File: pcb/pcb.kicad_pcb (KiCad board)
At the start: 2 copper layers, 11 parts, among them J1 pin_header, J2 power_jack_socket

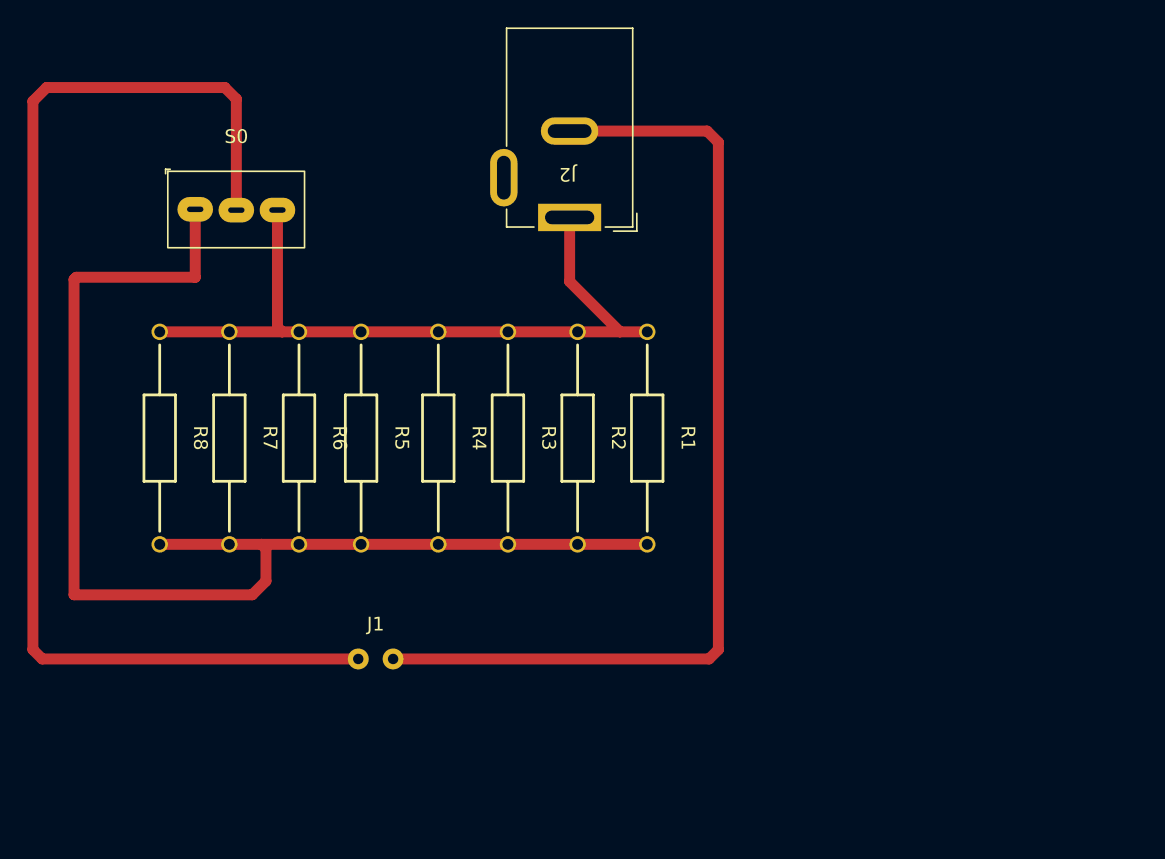
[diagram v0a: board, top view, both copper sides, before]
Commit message: add 3d render
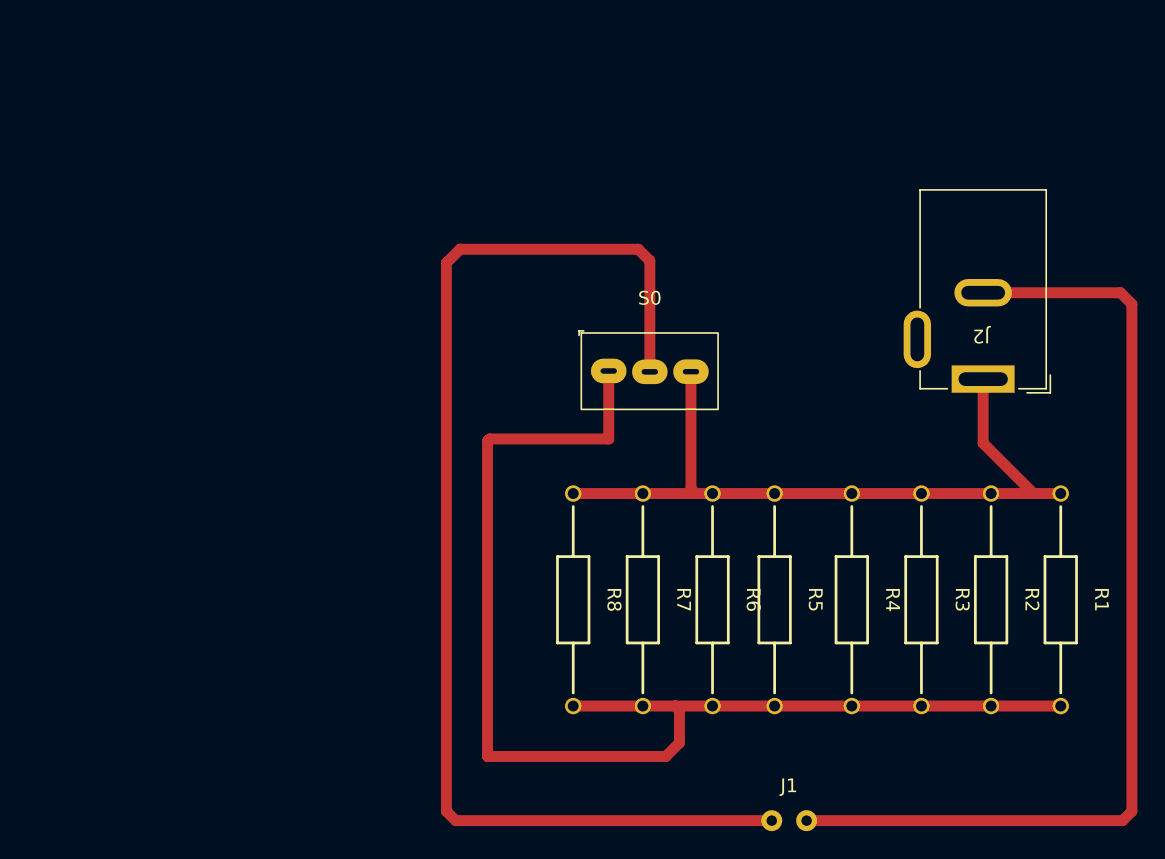
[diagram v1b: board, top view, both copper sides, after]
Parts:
- moved J2 32.4 mm to (171.4, 78.7)
- moved S0 32.4 mm to (147.0, 85.5)
- moved J1 32.4 mm to (157.2, 118.5)
- moved R1 32.4 mm to (176.9, 102.4)
- moved R2 32.4 mm to (171.9, 102.4)
- moved R3 32.4 mm to (166.8, 102.4)
- moved R4 32.4 mm to (161.7, 102.4)
- moved R5 32.4 mm to (156.1, 102.4)
- moved R6 32.4 mm to (151.5, 102.4)
- moved R8 32.4 mm to (141.4, 102.4)
- moved R7 32.4 mm to (146.5, 102.4)
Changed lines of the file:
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@@
   (net 5 "Net-(R1-Pad2)")
   (footprint "Library:100_ohm_resistor" (layer "F.Cu")
-    (at 141.7 90.56 -90)
+    (at 171.861956 102.353478 -90)
     (property "Sheetfile" "pcb.kicad_sch")
     (property "Sheetname" "")
@@
   )
   (footprint "Library:100_ohm_resistor" (layer "F.Cu")
-    (at 116.3 90.56 -90)
+    (at 146.461956 102.353478 -90)
     (property "Sheetfile" "pcb.kicad_sch")
     (property "Sheetname" "")
@@
   )
   (footprint "Library:100_ohm_resistor" (layer "F.Cu")
-    (at 121.38 90.56 -90)
+    (at 151.541956 102.353478 -90)
     (property "Sheetfile" "pcb.kicad_sch")
     (property "Sheetname" "")
@@
   )
   (footprint "Library:slide_switch" (layer "F.Cu")
-    (at 116.84 73.66)
+    (at 147.001956 85.453478)
     (property "Sheetfile" "pcb.kicad_sch")
     (property "Sheetname" "")
@@
   )
   (footprint "Library:100_ohm_resistor" (layer "F.Cu")
-    (at 131.54 90.56 -90)
+    (at 161.701956 102.353478 -90)
     (property "Sheetfile" "pcb.kicad_sch")
     (property "Sheetname" "")
@@
   )
   (footprint "Library:100_ohm_resistor" (layer "F.Cu")
-    (at 111.22 90.56 -90)
+    (at 141.381956 102.353478 -90)
     (property "Sheetfile" "pcb.kicad_sch")
     (property "Sheetname" "")
@@
   )
   (footprint "Library:100_ohm_resistor" (layer "F.Cu")
-    (at 136.62 90.56 -90)
+    (at 166.781956 102.353478 -90)
     (property "Sheetfile" "pcb.kicad_sch")
     (property "Sheetname" "")
@@
   )
   (footprint "Library:power_jack_socket" (layer "F.Cu")
-    (at 141.23 66.955 180)
+    (at 171.391956 78.748478 180)
     (property "Sheetfile" "pcb.kicad_sch")
     (property "Sheetname" "")
@@
   )
   (footprint "Library:100_ohm_resistor" (layer "F.Cu")
-    (at 146.78 90.56 -90)
+    (at 176.941956 102.353478 -90)
     (property "Sheetfile" "pcb.kicad_sch")
     (property "Sheetname" "")
@@
   )
   (footprint "Library:100_ohm_resistor" (layer "F.Cu")
-    (at 125.9092 90.56 -90)
+    (at 156.071156 102.353478 -90)
     (property "Sheetfile" "pcb.kicad_sch")
     (property "Sheetname" "")
@@
   )
   (footprint "Library:pin_header" (layer "F.Cu")
-    (at 127 106.68)
+    (at 157.161956 118.473478)
     (property "Sheetfile" "pcb.kicad_sch")
     (property "Sheetname" "")
@@
     )
   )
-  (gr_rect (start 99 63) (end 155 112) (layer "F.CrtYd") (width 0.05) (fill none))
-  (segment (start 116.8375 73.9425) (end 116.8375 65.8375) (width 0.8) (layer "F.Cu") (net 1))
-  (segment (start 103 65) (end 102 66) (width 0.8) (layer "F.Cu") (net 1))
-  (segment (start 102.68 106.68) (end 125.733 106.68) (width 0.8) (layer "F.Cu") (net 1))
-  (segment (start 116 65) (end 103 65) (width 0.8) (layer "F.Cu") (net 1))
-  (segment (start 116.8375 65.8375) (end 116 65) (width 0.8) (layer "F.Cu") (net 1))
-  (segment (start 102 66) (end 102 106) (width 0.8) (layer "F.Cu") (net 1))
-  (segment (start 102 106) (end 102.68 106.68) (width 0.8) (layer "F.Cu") (net 1))
-  (segment (start 152 69) (end 152 106) (width 0.8) (layer "F.Cu") (net 2))
-  (segment (start 141.15 68.175) (end 151.175 68.175) (width 0.8) (layer "F.Cu") (net 2))
-  (segment (start 151.175 68.175) (end 152 69) (width 0.8) (layer "F.Cu") (net 2))
-  (segment (start 151.32 106.68) (end 128.273 106.68) (width 0.8) (layer "F.Cu") (net 2))
-  (segment (start 152 106) (end 151.32 106.68) (width 0.8) (layer "F.Cu") (net 2))
-  (segment (start 120.18 82.82) (end 111.25 82.82) (width 0.8) (layer "F.Cu") (net 3))
-  (segment (start 119.838044 73.935) (end 119.838044 82.478044) (width 0.8) (layer "F.Cu") (net 3))
-  (segment (start 146.81 82.82) (end 144.82 82.82) (width 0.8) (layer "F.Cu") (net 3))
-  (segment (start 119.838044 82.478044) (end 120.18 82.82) (width 0.8) (layer "F.Cu") (net 3))
-  (segment (start 141.15 74.475) (end 141.15 79.15) (width 0.8) (layer "F.Cu") (net 3))
-  (segment (start 144.82 82.82) (end 120.18 82.82) (width 0.8) (layer "F.Cu") (net 3))
-  (segment (start 141.15 79.15) (end 144.82 82.82) (width 0.8) (layer "F.Cu") (net 3))
-  (segment (start 105.16 78.84) (end 105 79) (width 0.8) (layer "F.Cu") (net 5))
-  (segment (start 118 102) (end 119 101) (width 0.8) (layer "F.Cu") (net 5))
-  (segment (start 119 98.64) (end 118.68 98.32) (width 0.8) (layer "F.Cu") (net 5))
-  (segment (start 105 102) (end 118 102) (width 0.8) (layer "F.Cu") (net 5))
-  (segment (start 105 79) (end 105 102) (width 0.8) (layer "F.Cu") (net 5))
-  (segment (start 119 101) (end 119 98.64) (width 0.8) (layer "F.Cu") (net 5))
-  (segment (start 113.84 73.8825) (end 113.84 78.84) (width 0.8) (layer "F.Cu") (net 5))
-  (segment (start 146.81 98.32) (end 118.68 98.32) (width 0.8) (layer "F.Cu") (net 5))
-  (segment (start 113.84 78.84) (end 105.16 78.84) (width 0.8) (layer "F.Cu") (net 5))
-  (segment (start 118.68 98.32) (end 111.25 98.32) (width 0.8) (layer "F.Cu") (net 5))
+  (gr_rect (start 129.161956 74.793478) (end 185.161956 123.793478) (layer "F.CrtYd") (width 0.05) (fill none))
+  (segment (start 146.999456 85.735978) (end 146.999456 77.630978) (width 0.8) (layer "F.Cu") (net 1))
+  (segment (start 133.161956 76.793478) (end 132.161956 77.793478) (width 0.8) (layer "F.Cu") (net 1))
+  (segment (start 132.841956 118.473478) (end 155.894956 118.473478) (width 0.8) (layer "F.Cu") (net 1))
+  (segment (start 146.161956 76.793478) (end 133.161956 76.793478) (width 0.8) (layer "F.Cu") (net 1))
+  (segment (start 146.999456 77.630978) (end 146.161956 76.793478) (width 0.8) (layer "F.Cu") (net 1))
+  (segment (start 132.161956 77.793478) (end 132.161956 117.793478) (width 0.8) (layer "F.Cu") (net 1))
+  (segment (start 132.161956 117.793478) (end 132.841956 118.473478) (width 0.8) (layer "F.Cu") (net 1))
+  (segment (start 182.161956 80.793478) (end 182.161956 117.793478) (width 0.8) (layer "F.Cu") (net 2))
+  (segment (start 171.311956 79.968478) (end 181.336956 79.968478) (width 0.8) (layer "F.Cu") (net 2))
+  (segment (start 181.336956 79.968478) (end 182.161956 80.793478) (width 0.8) (layer "F.Cu") (net 2))
+  (segment (start 181.481956 118.473478) (end 158.434956 118.473478) (width 0.8) (layer "F.Cu") (net 2))
+  (segment (start 182.161956 117.793478) (end 181.481956 118.473478) (width 0.8) (layer "F.Cu") (net 2))
+  (segment (start 150.341956 94.613478) (end 141.411956 94.613478) (width 0.8) (layer "F.Cu") (net 3))
+  (segment (start 150 85.728478) (end 150 94.271522) (width 0.8) (layer "F.Cu") (net 3))
+  (segment (start 176.971956 94.613478) (end 174.981956 94.613478) (width 0.8) (layer "F.Cu") (net 3))
+  (segment (start 150 94.271522) (end 150.341956 94.613478) (width 0.8) (layer "F.Cu") (net 3))
+  (segment (start 171.311956 86.268478) (end 171.311956 90.943478) (width 0.8) (layer "F.Cu") (net 3))
+  (segment (start 174.981956 94.613478) (end 150.341956 94.613478) (width 0.8) (layer "F.Cu") (net 3))
+  (segment (start 171.311956 90.943478) (end 174.981956 94.613478) (width 0.8) (layer "F.Cu") (net 3))
+  (segment (start 135.321956 90.633478) (end 135.161956 90.793478) (width 0.8) (layer "F.Cu") (net 5))
+  (segment (start 148.161956 113.793478) (end 149.161956 112.793478) (width 0.8) (layer "F.Cu") (net 5))
+  (segment (start 149.161956 110.433478) (end 148.841956 110.113478) (width 0.8) (layer "F.Cu") (net 5))
+  (segment (start 135.161956 113.793478) (end 148.161956 113.793478) (width 0.8) (layer "F.Cu") (net 5))
+  (segment (start 135.161956 90.793478) (end 135.161956 113.793478) (width 0.8) (layer "F.Cu") (net 5))
+  (segment (start 149.161956 112.793478) (end 149.161956 110.433478) (width 0.8) (layer "F.Cu") (net 5))
+  (segment (start 144.001956 85.675978) (end 144.001956 90.633478) (width 0.8) (layer "F.Cu") (net 5))
+  (segment (start 176.971956 110.113478) (end 148.841956 110.113478) (width 0.8) (layer "F.Cu") (net 5))
+  (segment (start 144.001956 90.633478) (end 135.321956 90.633478) (width 0.8) (layer "F.Cu") (net 5))
+  (segment (start 148.841956 110.113478) (end 141.411956 110.113478) (width 0.8) (layer "F.Cu") (net 5))
 )
